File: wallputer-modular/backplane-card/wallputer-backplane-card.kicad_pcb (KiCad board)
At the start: 2 copper layers, 66 x 66 mm, 4 parts

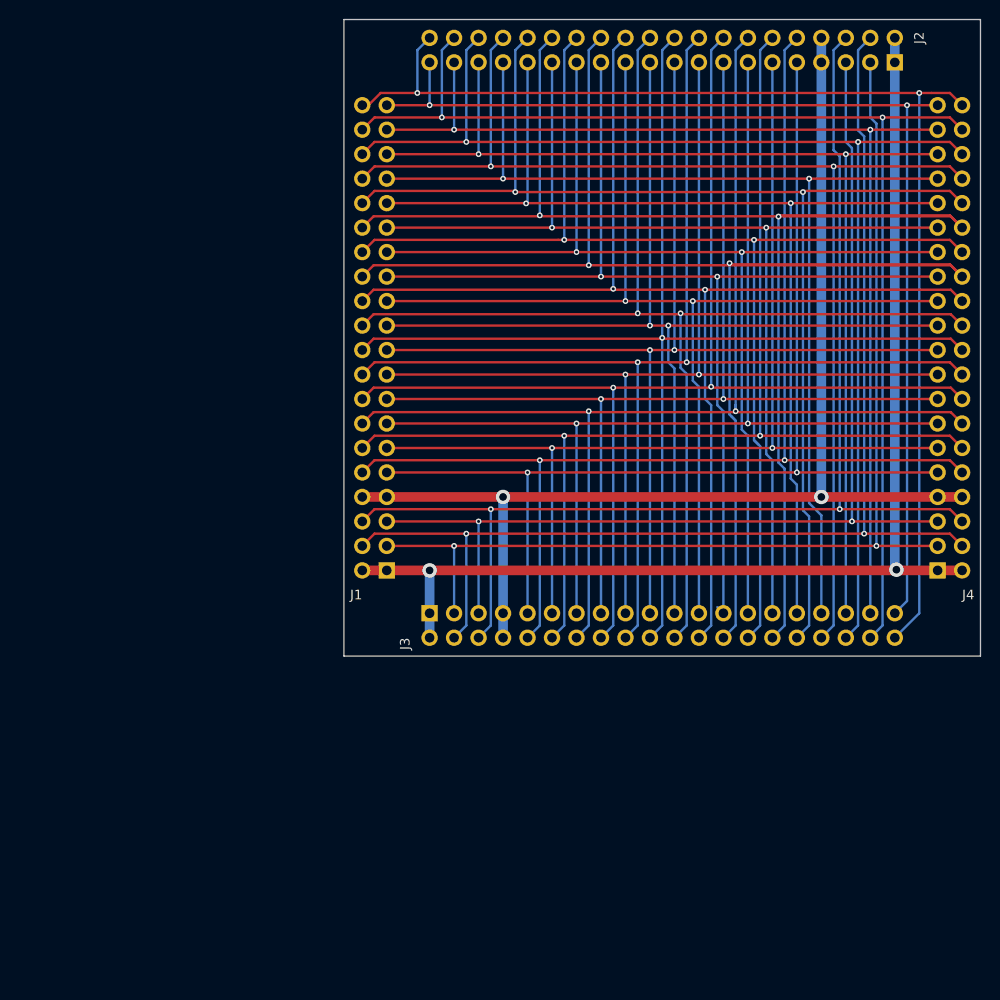
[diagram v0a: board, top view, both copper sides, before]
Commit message: resize backplane; add base card
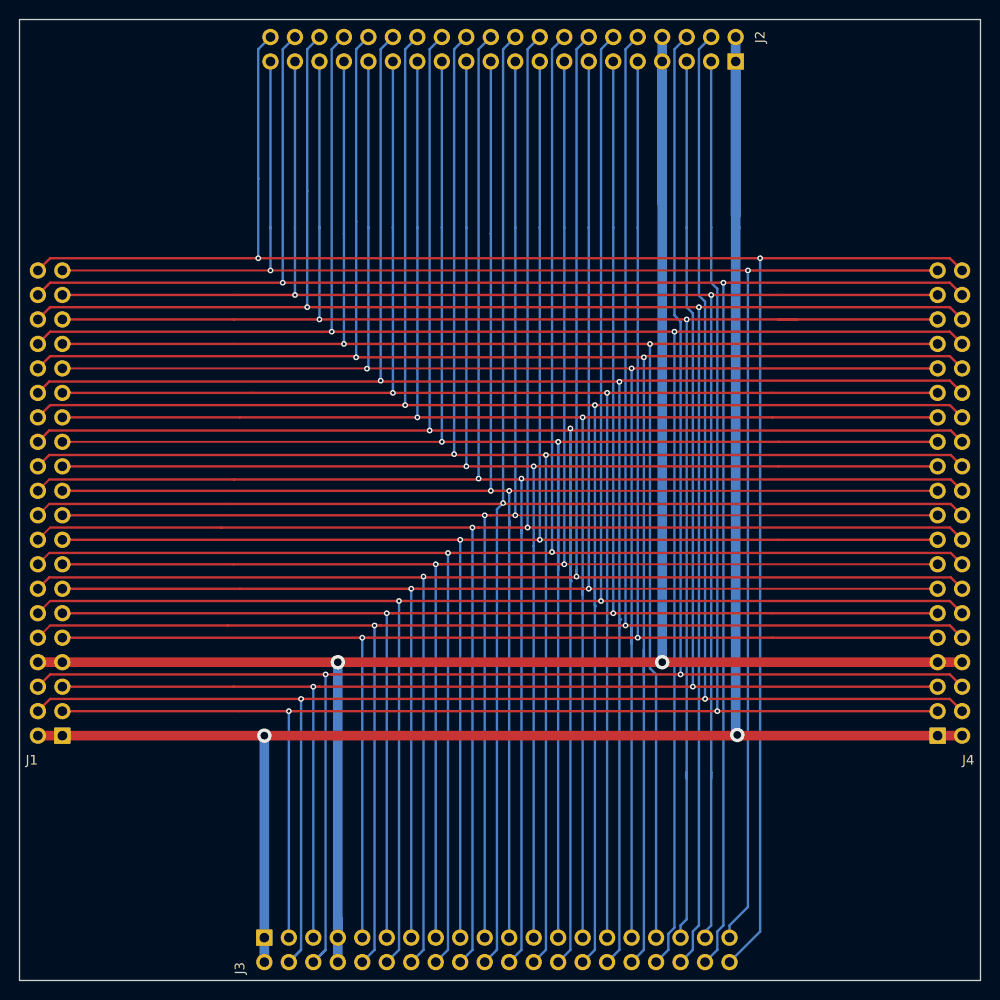
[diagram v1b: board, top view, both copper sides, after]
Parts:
- moved J3 37.8 mm to (64.1, 146.1)
- moved J1 37.8 mm to (43.2, 125.1)
- moved J4 17.1 mm to (134.0, 125.1)
- moved J2 16.5 mm to (113.0, 55.2)
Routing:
- net /+5V: track 124.5 -> 208.5 mm
- net /Vss: track 124.5 -> 207.8 mm
- net /D7: track 115.5 -> 195.0 mm
- net /D2: track 114.3 -> 184.5 mm
- net /A11: track 126.9 -> 196.7 mm
- net /A9: track 127.4 -> 197.1 mm
- net /NC2: track 126.7 -> 196.0 mm
- net /NC3: track 126.8 -> 196.0 mm
- net /D4: track 114.7 -> 183.7 mm
- net /D1: track 114.3 -> 182.6 mm
- net /A14: track 126.6 -> 194.3 mm
- net /D6: track 114.6 -> 182.3 mm
- net /NC30: track 114.6 -> 182.3 mm
- net /A6: track 126.7 -> 194.5 mm
- net /A13: track 126.4 -> 194.1 mm
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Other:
- board size 66 x 66 mm -> 99.7 x 99.7 mm
